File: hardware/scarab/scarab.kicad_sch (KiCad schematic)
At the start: 21 parts, among them J1 Conn_01x02_Male-Connector, J2 Conn_01x08_Male, J3 Conn_01x02, U2 AP2205-33Y-13, U3 ATTiny1616-MNR

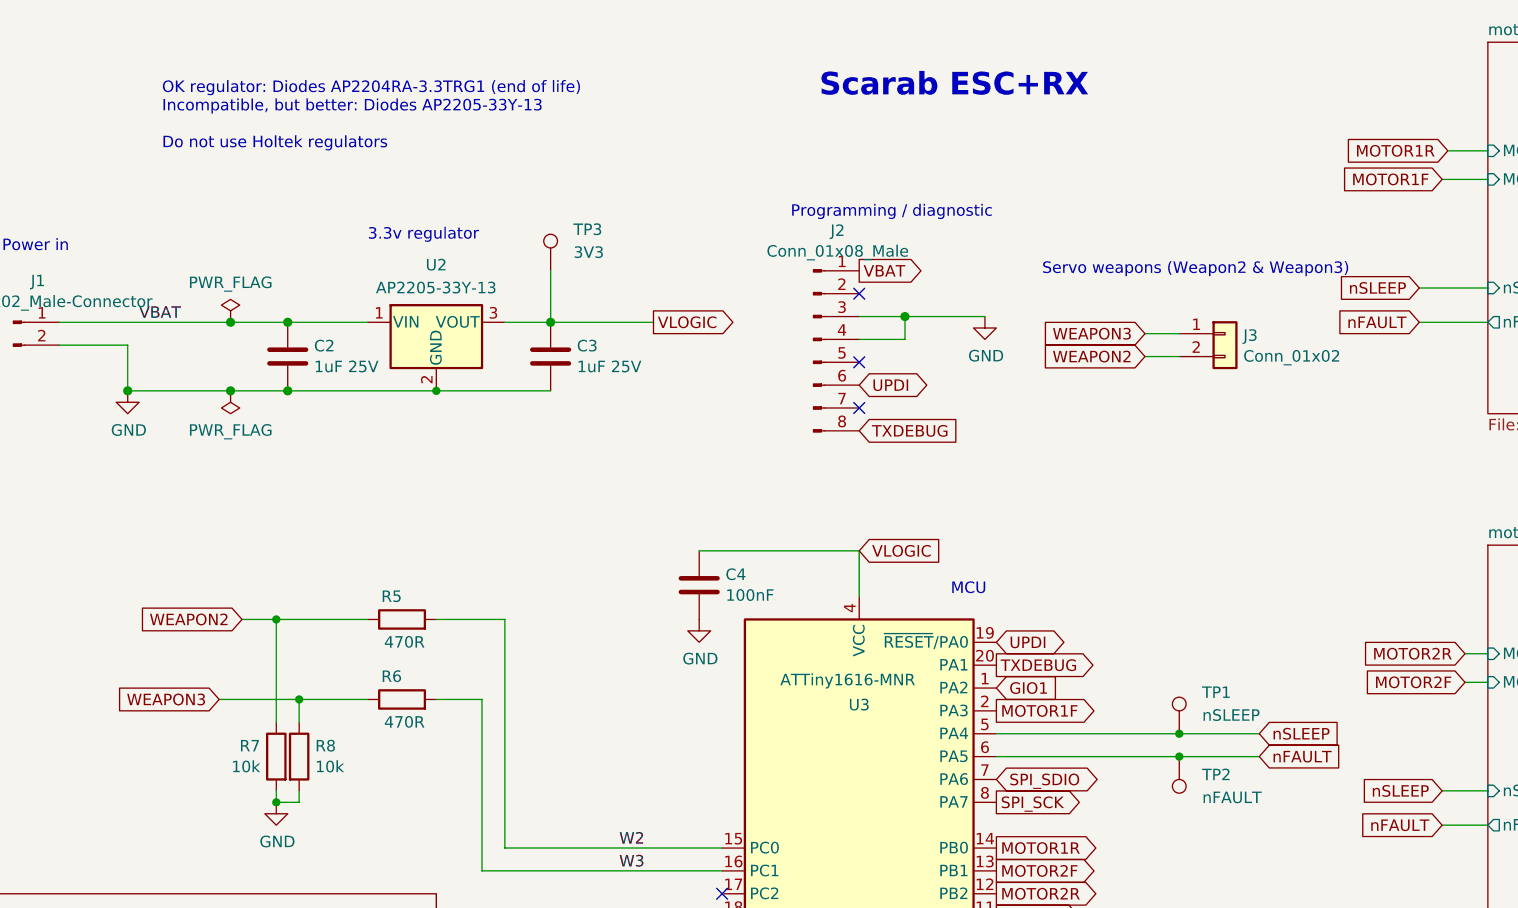
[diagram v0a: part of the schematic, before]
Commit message: Scarab schematic cosmetic fixes
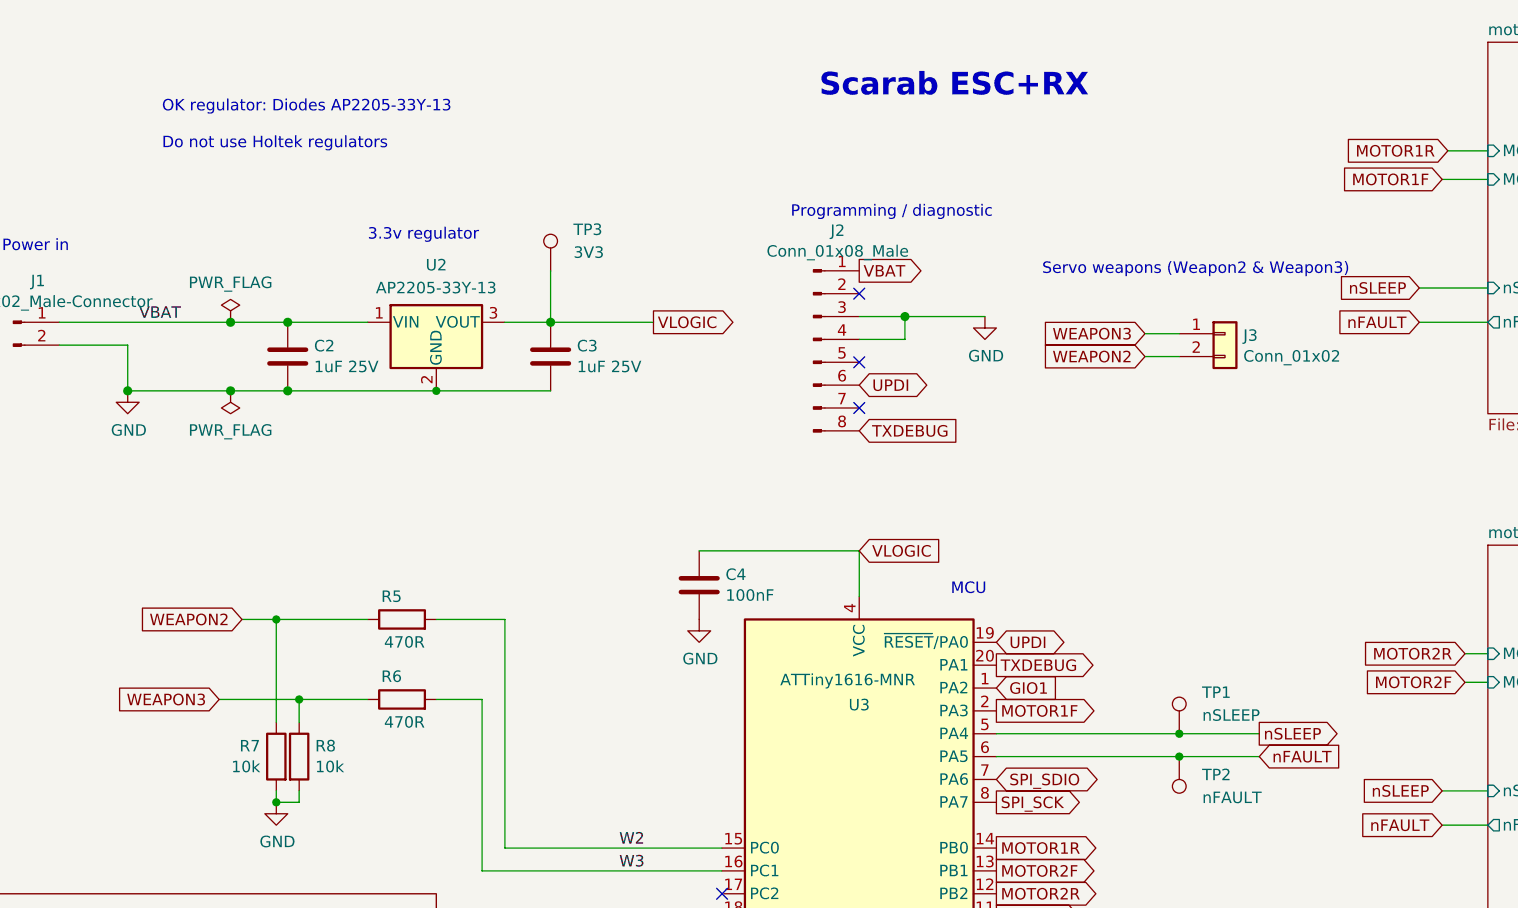
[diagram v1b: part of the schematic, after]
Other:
- note added: "${TITLE}"
- note added: "OK regulator: Diodes AP2205-33Y-13 Do not use Holtek regulators"
- note removed: "OK regulator: Diodes AP2204RA-3.3TRG1 (end of life) Incompatible, but better: Diodes AP2205-33Y-13 Do not use Holtek regulators"
- note removed: "Scarab ESC+RX"
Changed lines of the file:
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@@
     (effects (font (size 1.27 1.27)) (justify left bottom))
   )
-  (text "Scarab ESC+RX" (at 122.555 23.495 0)
+  (text "${TITLE}" (at 122.555 23.495 0)
     (effects (font (size 2.5 2.5) (thickness 0.5) bold) (justify left bottom))
   )
-  (text "OK regulator: Diodes AP2204RA-3.3TRG1 (end of life)\nIncompatible, but better: Diodes AP2205-33Y-13\n\nDo not use Holtek regulators"
+  (text "OK regulator: Diodes AP2205-33Y-13\n\nDo not use Holtek regulators"
     (at 49.53 29.21 0)
     (effects (font (size 1.27 1.27)) (justify left bottom))
@@
     )
   )
-  (global_label "nSLEEP" (shape input) (at 171.45 93.98 0) (fields_autoplaced)
+  (global_label "nSLEEP" (shape output) (at 171.45 93.98 0) (fields_autoplaced)
     (effects (font (size 1.27 1.27)) (justify left))
     (property "Intersheetrefs" "${INTERSHEET_REFS}" (at 181.4849 93.98 0)

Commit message: Schematic notes
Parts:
- added C8: 100nF, Capacitor_SMD:C_0402_1005Metric_Pad0.74x0.62mm_HandSolder, symbol Device:C
- added R14: 47R, Resistor_SMD:R_0402_1005Metric, symbol Device:R
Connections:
- net GND: now also C8.2
- net VBAT: now also R14.1; no longer C2.1, U2.1 (VIN)
- net VSENSE: now also C8.1
- new net: C2.1, R14.2, U2.1 (VIN)
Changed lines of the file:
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@@
     (stroke (width 0) (type default))
   )
-  (wire (pts (xy 38.1 48.26) (xy 57.15 48.26))
+  (wire (pts (xy 38.1 48.26) (xy 45.72 48.26))
     (stroke (width 0) (type solid))
   )
@@
     (stroke (width 0) (type default))
   )
+  (wire (pts (xy 53.34 48.26) (xy 57.15 48.26))
+    (stroke (width 0) (type solid))
+  )
   (wire (pts (xy 191.77 100.33) (xy 196.85 100.33))
     (stroke (width 0) (type default))
@@
     (stroke (width 0) (type solid))
   )
+  (wire (pts (xy 99.695 156.21) (xy 106.68 156.21))
+    (stroke (width 0) (type default))
+  )
   (wire (pts (xy 57.15 55.88) (xy 63.5 55.88))
     (stroke (width 0) (type solid))
@@
     (stroke (width 0) (type solid))
   )
-  (text "Voltage sense" (at 102.87 151.13 90)
+  (text "Voltage sense" (at 96.52 144.145 90)
     (effects (font (size 1.27 1.27)) (justify right bottom))
   )
@@
     (effects (font (size 1.27 1.27)) (justify left bottom))
   )
-  (label "VBAT" (at 46.99 48.26 0) (fields_autoplaced)
+  (label "VBAT" (at 40.64 48.26 0) (fields_autoplaced)
     (effects (font (size 1.27 1.27)) (justify left bottom))
   )
@@
     (property "Intersheetrefs" "${INTERSHEET_REFS}" (at -59.69 22.225 0)
       (effects (font (size 1.27 1.27)) hide)
+    )
+  )
+  (symbol (lib_id "Device:R") (at 49.53 48.26 90) (unit 1)
+    (in_bom yes) (on_board yes) (dnp no)
+    (property "Reference" "R14" (at 49.53 45.72 90)
+      (effects (font (size 1.27 1.27)) (justify left))
+    )
+    (property "Value" "47R" (at 52.07 50.8 90)
+      (effects (font (size 1.27 1.27)) (justify left))
+    )
+    (property "Footprint" "Resistor_SMD:R_0402_1005Metric" (at 49.53 50.038 90)
+      (effects (font (size 1.27 1.27)) hide)
+    )
+    (property "Datasheet" "~" (at 49.53 48.26 0)
+      (effects (font (size 1.27 1.27)) hide)
+    )
+    (property "LCSC" "" (at 49.53 48.26 0)
+      (effects (font (size 1.27 1.27)) hide)
+    )
+    (property "Manufacturer" "Uniroyal" (at 49.53 48.26 0)
+      (effects (font (size 1.27 1.27)) hide)
+    )
+    (property "PartNumber" "" (at 49.53 48.26 0)
+      (effects (font (size 1.27 1.27)) hide)
+    )
+    (pin "1")
+    (pin "2")
+    (instances
+      (project "scarab"
+        (path "/f41619e3-8cf2-4511-8a51-762d4de43197"
+          (reference "R14") (unit 1)
+        )
+      )
     )
   )
@@
     )
     (property "Value" "Conn_01x02_Male-Connector" (at 35.7632 45.974 0)
-      (effects (font (size 1.27 1.27)))
+      (effects (font (size 1.27 1.27)) hide)
     )
     (property "Footprint" "malenki-nano:beetlepower" (at 33.02 48.26 0)
@@
         (path "/f41619e3-8cf2-4511-8a51-762d4de43197"
           (reference "D1") (unit 1)
+        )
+      )
+    )
+  )
+  (symbol (lib_id "Device:C") (at 99.695 160.02 0) (mirror y) (unit 1)
+    (in_bom yes) (on_board yes) (dnp no)
+    (property "Reference" "C8" (at 96.774 158.8516 0)
+      (effects (font (size 1.27 1.27)) (justify left))
+    )
+    (property "Value" "100nF" (at 96.774 161.163 0)
+      (effects (font (size 1.27 1.27)) (justify left))
+    )
+    (property "Footprint" "Capacitor_SMD:C_0402_1005Metric_Pad0.74x0.62mm_HandSolder" (at 98.7298 163.83 0)
+      (effects (font (size 1.27 1.27)) hide)
+    )
+    (property "Datasheet" "~" (at 99.695 160.02 0)
+      (effects (font (size 1.27 1.27)) hide)
+    )
+    (property "LCSC" "C307331" (at 99.695 160.02 0)
+      (effects (font (size 1.27 1.27)) hide)
+    )
+    (property "Manufacturer" "Samsung" (at 99.695 160.02 0)
+      (effects (font (size 1.27 1.27)) hide)
+    )
+    (property "PartNumber" "" (at 99.695 160.02 0)
+      (effects (font (size 1.27 1.27)) hide)
+    )
+    (pin "1")
+    (pin "2")
+    (instances
+      (project "scarab"
+        (path "/f41619e3-8cf2-4511-8a51-762d4de43197"
+          (reference "C8") (unit 1)
         )
       )
@@
         )
       )
+    )
+  )
+  (symbol (lib_id "power:GND") (at 99.695 163.83 0) (unit 1)
+    (in_bom yes) (on_board yes) (dnp no)
+    (property "Reference" "#PWR033" (at 99.695 170.18 0)
+      (effects (font (size 1.27 1.27)) hide)
+    )
+    (property "Value" "GND" (at 99.822 168.2242 0)
+      (effects (font (size 1.27 1.27)))
+    )
+    (property "Footprint" "" (at 99.695 163.83 0)
+      (effects (font (size 1.27 1.27)) hide)
+    )
+    (property "Datasheet" "" (at 99.695 163.83 0)
+      (effects (font (size 1.27 1.27)) hide)
+    )
+    (pin "1")
+    (instances
+      (project "scarab"
+        (path "/f41619e3-8cf2-4511-8a51-762d4de43197"
+          (reference "#PWR033") (unit 1)
+        )
+      )

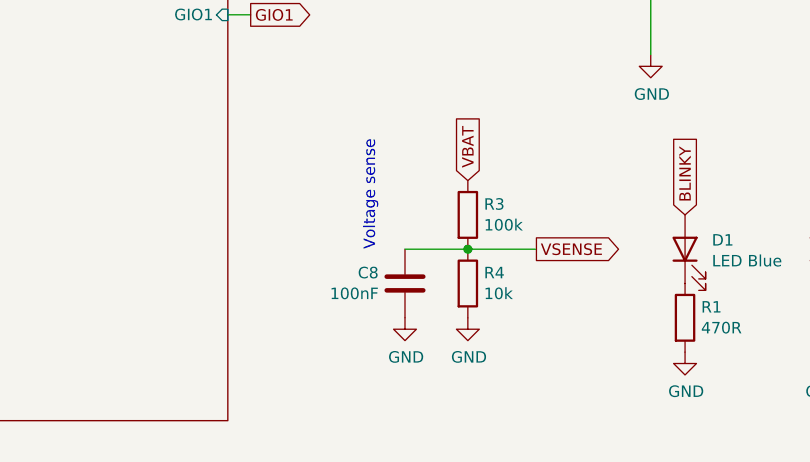
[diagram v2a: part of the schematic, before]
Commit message: Scarab: tidy up dnp parts on board
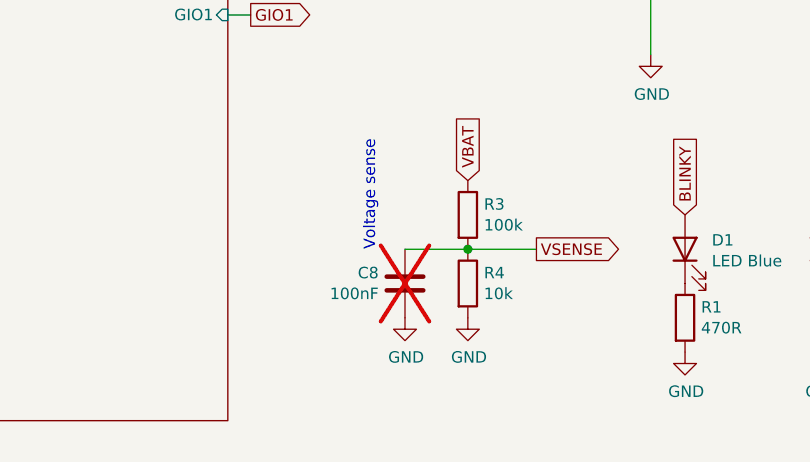
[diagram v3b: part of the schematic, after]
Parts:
- C8: now not fitted; now left out of the parts list
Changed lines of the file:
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@@
   )
   (symbol (lib_id "Device:C") (at 99.695 160.02 0) (mirror y) (unit 1)
-    (in_bom yes) (on_board yes) (dnp no)
+    (in_bom no) (on_board yes) (dnp yes)
     (property "Reference" "C8" (at 96.774 158.8516 0)
       (effects (font (size 1.27 1.27)) (justify left))
